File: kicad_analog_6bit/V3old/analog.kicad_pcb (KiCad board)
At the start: 2 copper layers, 50 x 23.2 mm, 30 parts, among them P1 Conn_02x05_Odd_Even, P2 Conn_01x04, P3 Conn_01x06, P4 Conn_01x02, P6 Conn_01x01, P7 Conn_01x01, U1 MAX9144, U2 MAX9144, U3 DG441xY, U4 MAX5259EEE+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

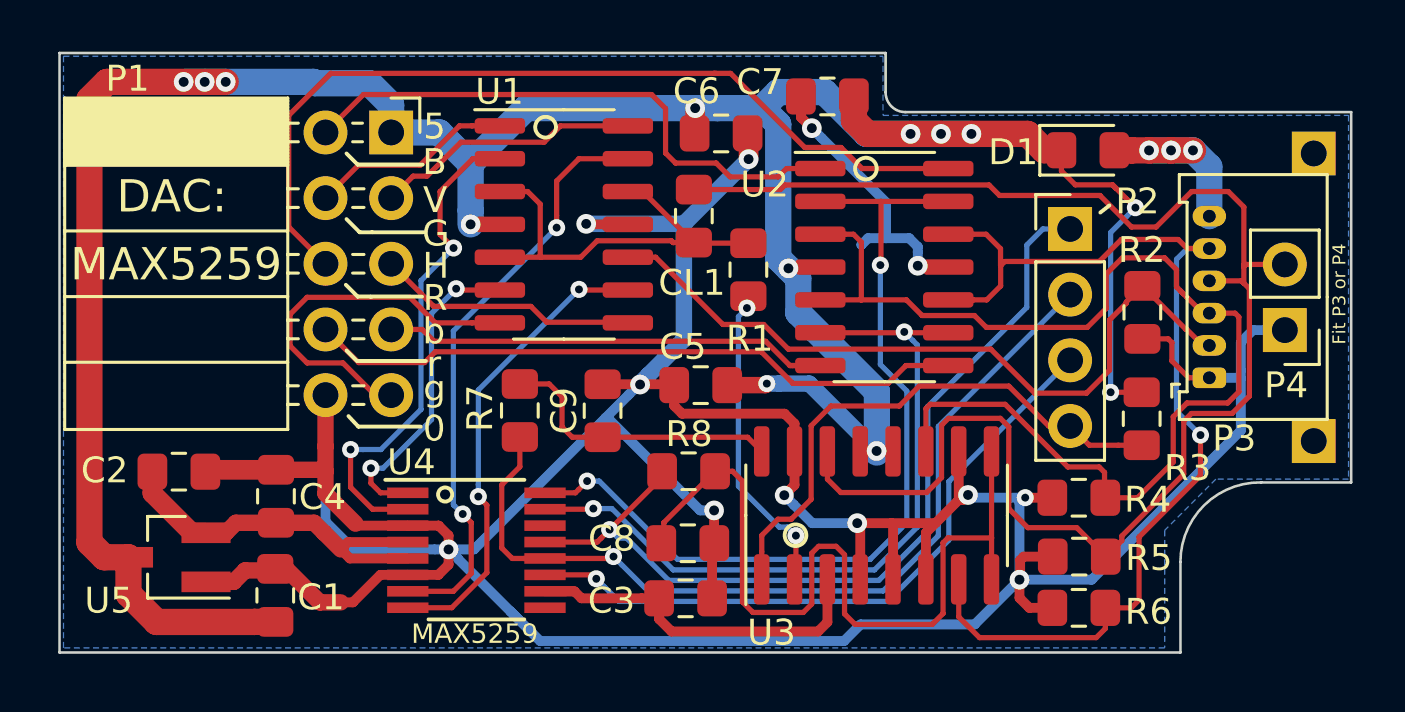
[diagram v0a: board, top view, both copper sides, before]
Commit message: Update issue 3 with normally closed DG441
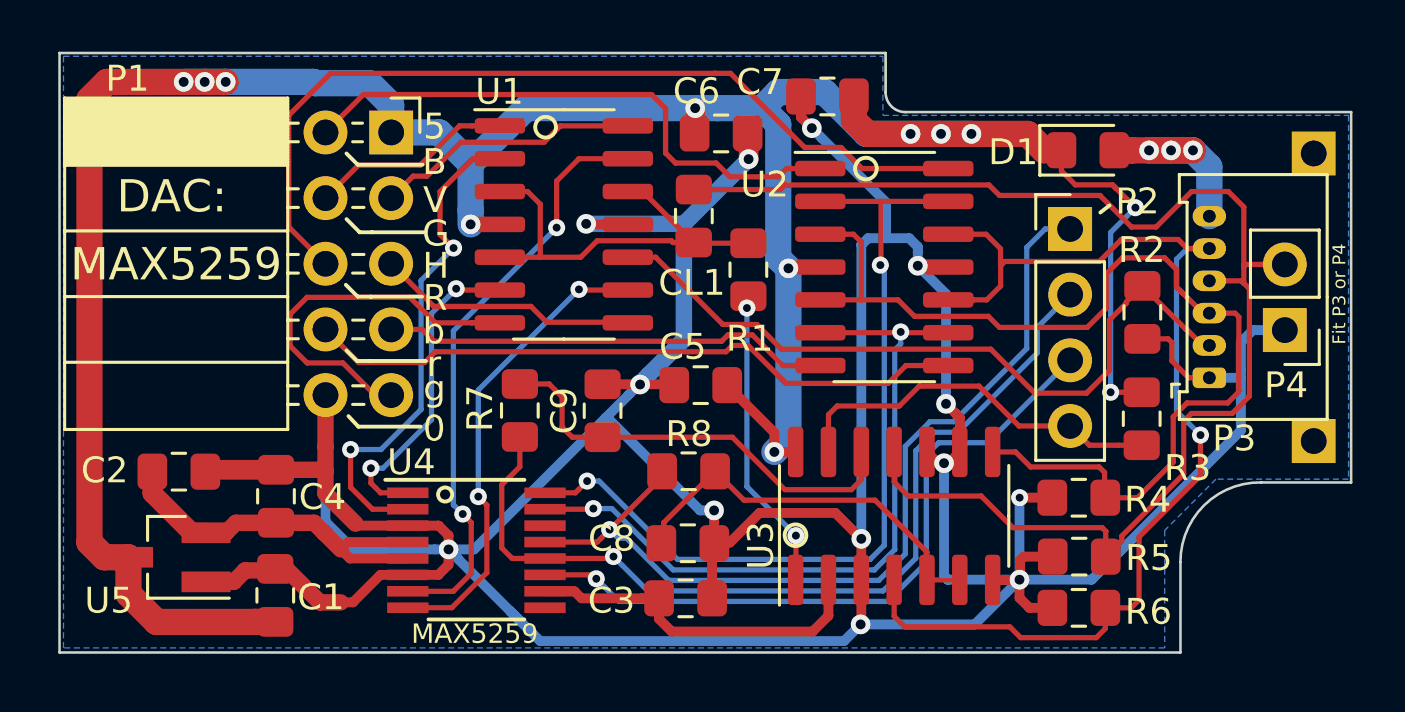
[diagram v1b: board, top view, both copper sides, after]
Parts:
- R7, R8: value 10K -> 100K
- U3: value DG441xY -> 4066; footprint Package_SO:SOIC-16_3.9x9.9mm_P1.27mm -> Package_SO:SOIC-14_3.9x8.7mm_P1.27mm
- moved U3 0.68 mm to (59.8, 49.2)
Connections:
- U3 pad 1: /CLAMP -> /SW_CLAMP
- U3 pad 11: /ABLUE -> /AGREEN
- U3 pad 12: /VCC -> /TERM_G
- U3 pad 13: /VCC -> /CLAMP
- U3 pad 14: /AGREEN -> /VCC
- U3 pad 2: /SW_CLAMP -> /CLAMPLVL
- U3 pad 3: /CLAMPLVL -> /GND
- U3 pad 4: /GND -> /ARED
- U3 pad 5: /GND -> /TERM_RB
- U3 pad 6: /GND -> /TERM_RB
- U3 pad 7: /ARED -> /GND
- U3 pad 8: /TERM_RB -> /ABLUE
- U3 pad 9: /TERM_RB -> /GND
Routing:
- net /TERM_RB: track 32.1 -> 15.5 mm
- net /GND: track 168.8 -> 181.4 mm, vias 12 -> 13
- net /AGREEN: track 61.4 -> 54.0 mm
- net /CLAMP: track 21.4 -> 15.0 mm
- net /TERM_G: track 11.1 -> 16.8 mm
- net /ABLUE: track 46.4 -> 41.3 mm
- net /VCC: track 117.8 -> 113.1 mm, vias 13 -> 12
- net /ARED: track 42.6 -> 45.0 mm
- net /GPIO22_STB: track 25.9 -> 27.0 mm
- net /REFRBUVHI: track 33.8 -> 33.1 mm
- net /REFRBUVLO: track 29.0 -> 28.4 mm
- net /GPIO1_CLK: track 35.4 -> 35.9 mm
